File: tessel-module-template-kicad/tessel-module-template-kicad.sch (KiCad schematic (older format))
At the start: 1 part

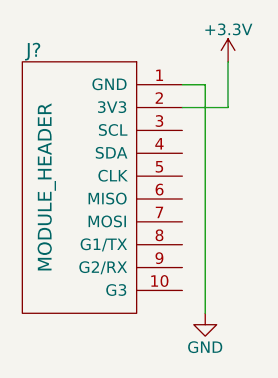
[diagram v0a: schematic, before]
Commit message: annotated schematic with first free number (ok for small, single-page designs; otherwise we typically use the 100 option)
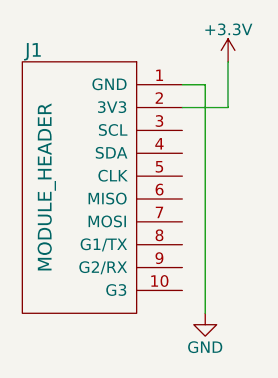
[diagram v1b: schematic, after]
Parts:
- gave numbers to parts that had none: 1
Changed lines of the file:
@@
 $EndDescr
 $Comp
-L MODULE_HEADER J?
+L MODULE_HEADER J1
 U 1 1 55C071A6
 P 4200 4000
-F 0 "J?" H 3850 4550 60  0000 C CNN
+F 0 "J1" H 3850 4550 60  0000 C CNN
 F 1 "MODULE_HEADER" V 3900 3950 60  0000 C CNN
 F 2 "" H 4200 4000 60  0000 C CNN
@@
 	4600 3600 4600 4600
 $Comp
-L GND #PWR?
+L GND #PWR1
 U 1 1 55C071C5
 P 4600 4600
-F 0 "#PWR?" H 4600 4350 50  0001 C CNN
+F 0 "#PWR1" H 4600 4350 50  0001 C CNN
 F 1 "GND" H 4600 4450 50  0000 C CNN
 F 2 "" H 4600 4600 60  0000 C CNN
@@
 $EndComp
 $Comp
-L +3.3V #PWR?
+L +3.3V #PWR2
 U 1 1 55C071DB
 P 4700 3500
-F 0 "#PWR?" H 4700 3350 50  0001 C CNN
+F 0 "#PWR2" H 4700 3350 50  0001 C CNN
 F 1 "+3.3V" H 4700 3640 50  0000 C CNN
 F 2 "" H 4700 3500 60  0000 C CNN

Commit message: assigned the module port a footprint
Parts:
- J1: footprint (none) -> tm-kicad-lib:MODULE_HEADER_MODULE
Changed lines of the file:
@@
 F 0 "J1" H 3850 4550 60  0000 C CNN
 F 1 "MODULE_HEADER" V 3900 3950 60  0000 C CNN
-F 2 "" H 4200 4000 60  0000 C CNN
+F 2 "tm-kicad-lib:MODULE_HEADER_MODULE" H 4200 4000 60  0001 C CNN
 F 3 "" H 4200 4000 60  0000 C CNN
 	1    4200 4000
@@
 	4600 3600 4600 4600
 $Comp
-L GND #PWR1
+L GND #PWR01
 U 1 1 55C071C5
 P 4600 4600
-F 0 "#PWR1" H 4600 4350 50  0001 C CNN
+F 0 "#PWR01" H 4600 4350 50  0001 C CNN
 F 1 "GND" H 4600 4450 50  0000 C CNN
 F 2 "" H 4600 4600 60  0000 C CNN
@@
 $EndComp
 $Comp
-L +3.3V #PWR2
+L +3.3V #PWR02
 U 1 1 55C071DB
 P 4700 3500
-F 0 "#PWR2" H 4700 3350 50  0001 C CNN
+F 0 "#PWR02" H 4700 3350 50  0001 C CNN
 F 1 "+3.3V" H 4700 3640 50  0000 C CNN
 F 2 "" H 4700 3500 60  0000 C CNN
